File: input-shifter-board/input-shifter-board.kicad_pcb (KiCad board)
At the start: 2 copper layers, 80 x 80 mm, 145 parts, among them J1 BUTTON1, J10 BUTTON10, J11 BUTTON11, J12 BUTTON12, J13 BUTTON13, J14 BUTTON14, J15 BUTTON15, J16 BUTTON16, J17 BUTTON17, J18 BUTTON18, J19 BUTTON19, J2 BUTTON2, J20 BUTTON20, J21 BUTTON21, J22 BUTTON22, J23 BUTTON23, J24 BUTTON24, J25 BUTTON25, J26 BUTTON26, J27 BUTTON27, J28 BUTTON28, J29 BUTTON29, J3 BUTTON3, J30 BUTTON30, J31 BUTTON31, J32 BUTTON32, J33 Data, J4 BUTTON4, J5 BUTTON5, J6 BUTTON6, J7 BUTTON7, J8 BUTTON8, J9 BUTTON9, U1 74HC165, U2 74HC165, U3 74HC165, U4 74HC165

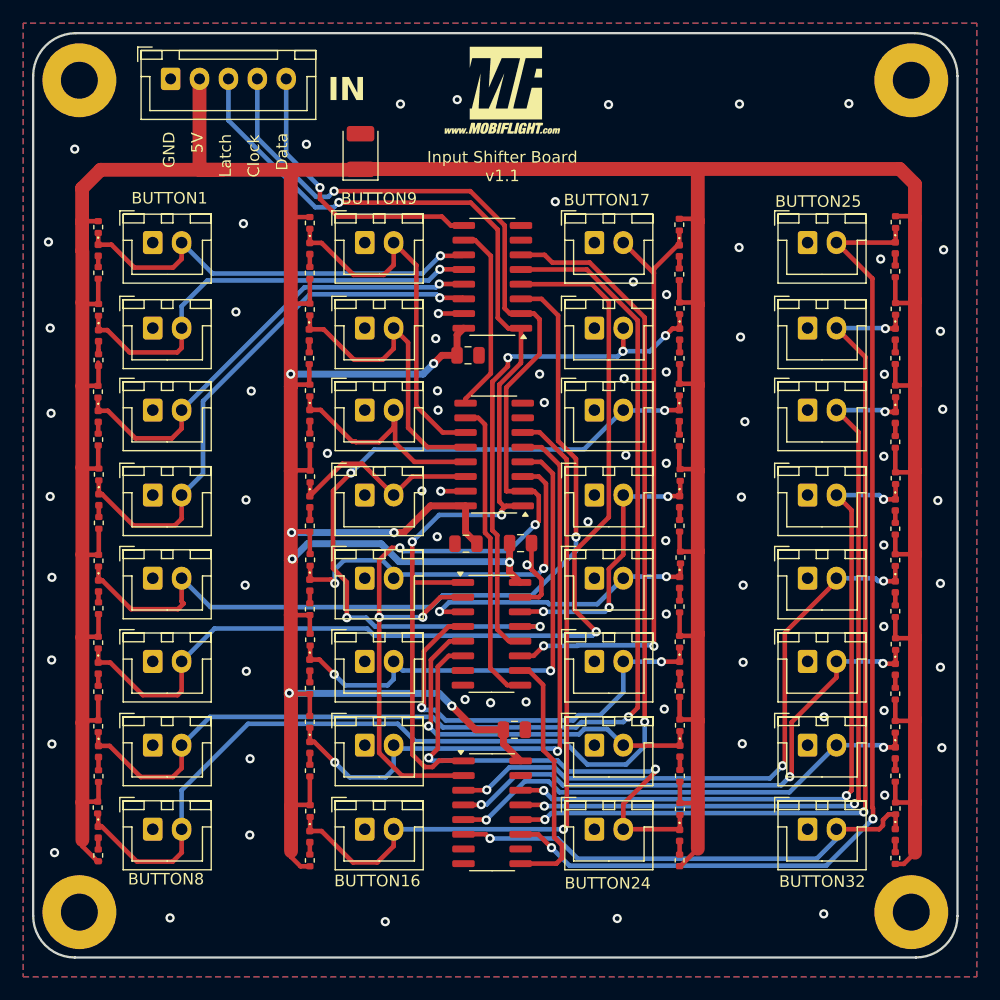
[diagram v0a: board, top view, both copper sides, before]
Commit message: Update all boards to KiCad 9.0 (#44)
* update dimmer board to KiCad version 9

* update dual encoder board to KiCad version 9

* update input shifter board, start numbering with zero instead one

* update MAX7219 breakout board to KiCad version 9

* add 3 pol JST connector

* updatge template to KiCad version 9

* update potentiometer board to KiCad version 9, use JST connector from MF lib

* update 6pin JST connector

* update prototyping board to KiCad version 9

* update symbols on dimmer board, fixed DRC

* update symbols from MAX7219 breakout board

* add Screw Terminalblocks to footprint lib and 3D models

* use screw terminals from MF lib

* fixed outline of Potentiometer board

* fixed missing IDC footprints error

* add MAX7219 symbol

* use MAX7219 symbol from MF lib

* add Mega2560mini symbol and footprint to MF library

* use Mega2560mini symbol and footprint from MF library

* add used Dual Encoder symbol and footprint to MF lib

* use footprint and symbol for Dual Encoder from MF lib
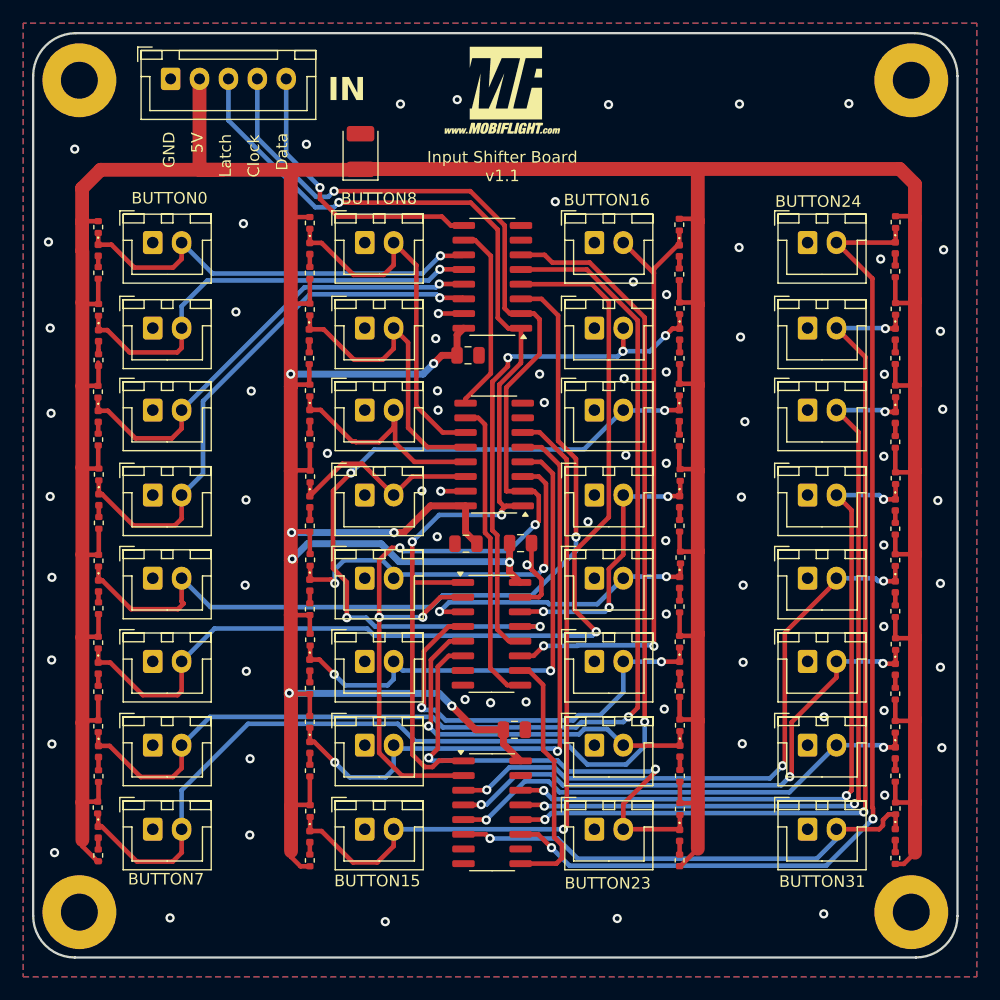
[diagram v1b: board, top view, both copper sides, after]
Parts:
- J1: value BUTTON1 -> BUTTON0
- J16: value BUTTON16 -> BUTTON15
- J17: value BUTTON17 -> BUTTON16
- J24: value BUTTON24 -> BUTTON23
- J25: value BUTTON25 -> BUTTON24
- J32: value BUTTON32 -> BUTTON31
- J8: value BUTTON8 -> BUTTON7
- J9: value BUTTON9 -> BUTTON8
- R13: value 70 -> 470
